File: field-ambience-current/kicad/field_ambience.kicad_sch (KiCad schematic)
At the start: 0 parts

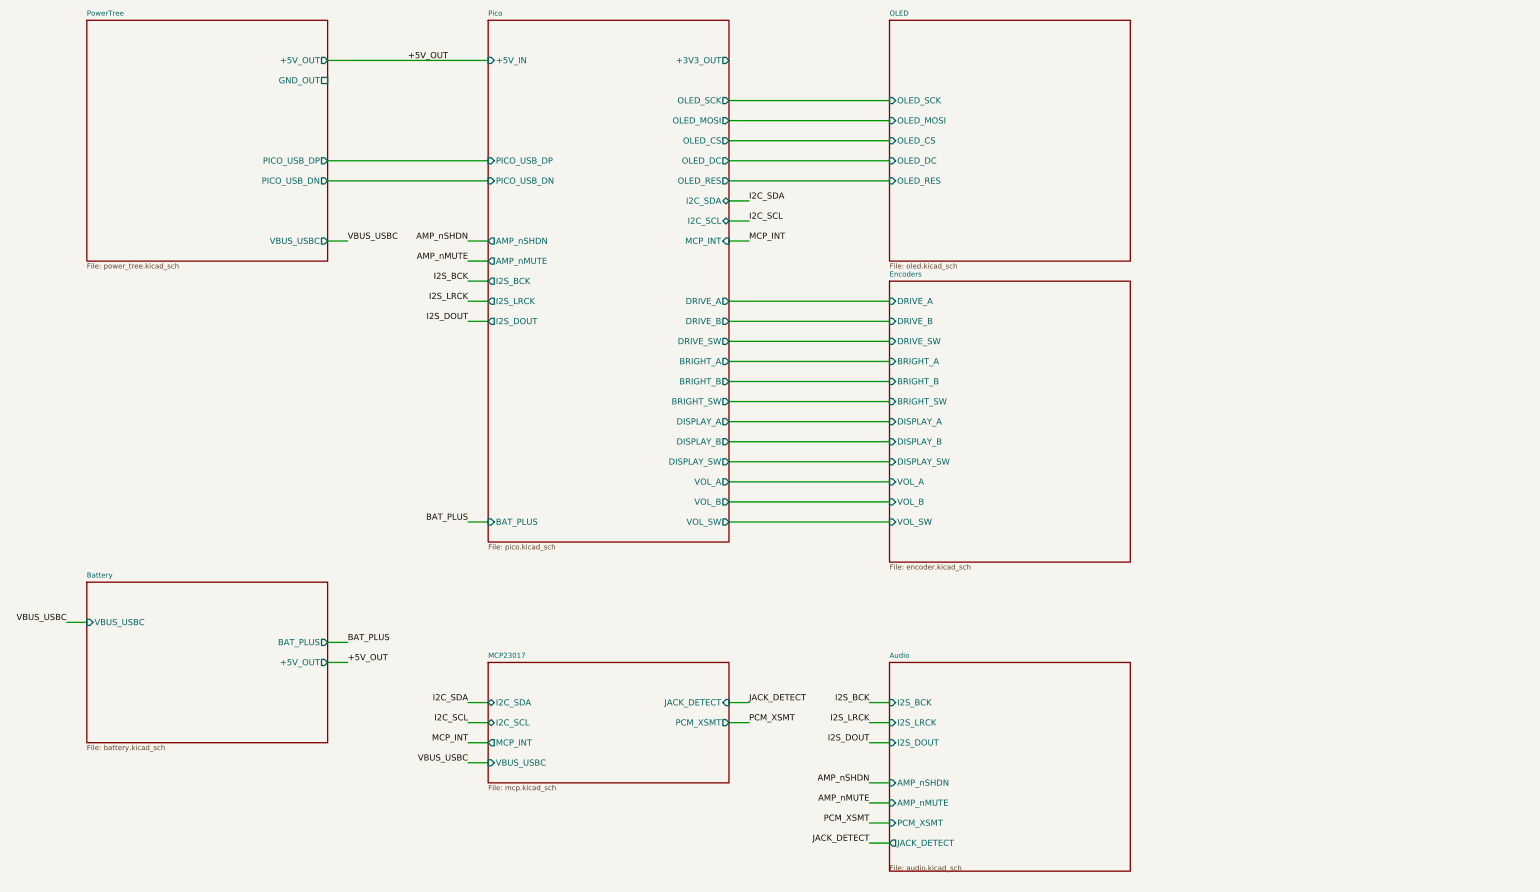
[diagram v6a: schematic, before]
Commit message: pcb(r18.5): Schematic-Migration Phase 3 — STM32H743 + LCD im Generator, Repo-Audit-Fixes
KERN: generate_kicad_project.py erzeugt jetzt die H7-Architektur.

NEU stm32h743.kicad_sch (ersetzt pico.kicad_sch -> kicad/legacy_pico2/):
- 100-Pin-Symbol 1:1 aus offizieller KiCad-Lib (MCU_ST_STM32H7),
  doppelt verifiziert gegen SPEC v0.7 §5 / DS12110 Rev 5 Table 8 —
  alle 52 belegten Zuordnungen identisch (zwei unabhängige Quellen)
- alle SPEC-§5-Netze verdrahtet, 48 Reserve-GPIOs no_connect
- Support: HSE Y1 ABLS-8.000MHZ-B4-T (C596838) + 2x22pF, VCAP 2x2.2uF
  (DS12110 Tab.24), 5x(4.7uF+100nF) VDD-Bank, VDDA-Ferrit C84094 +
  1uF+100nF, BOOT0-PD 10k, NRST-PU 10k+100nF, SWD-J4 (PA13/PA14/GND),
  BAT-Teiler 100k/100k+10nF an PA3, Status-LED PD8, USB-FS PA11/PA12
  (USBLC6-ESD bleibt davor), MIDI_TX-Netz (PD5)

NEU lcd.kicad_sch (ersetzt oled.kicad_sch -> legacy): 8-Pin-ST7789
per SPEC §6 + C6b/C6c + Backlight: PCA9685-Kanal-12 -> LCD_BLK_PWM ->
2N7002 Low-Side + 100k-PD. Netze OLED_* -> LCD_*.

power_tree: U5 AP7361A-33 LDO (+5V->+3V3) + Cin 1uF/Cout 2.2uF +
EN->IN. Pico-SMPS entfällt. PICO_USB_* -> USB_DM/USB_DP.

mcp: GPB5 = VOL_SW (SPEC §5.4 — lag bis r17 entgegen der SPEC am
Pico-GPIO), PCA-Kanal 12 = LCD_BLK_PWM. Root-Brücken umgebaut,
kicad_pro-Sheetliste: Battery ergänzt (fehlte).

AUDIT-FINDINGS (verifiziert, nicht aus dem Alt-Audit übernommen):
- F-6 NEU 🔴: SPEC-§4-U5-LCSC C156144 ist ein 910R-WIDERSTAND
  (LCSC-Web verifiziert) — hätte bei JLC einen R als LDO bestückt.
  SPEC korrigiert (Kandidat C150719), Symbol trägt TBD-VERIFY.
- B-LDO 🔴: AP7361A-SOT-89-5-Pinout-Annahme (1=ADJ/NC,2=OUT,3=IN,
  4=GND,5=EN aus AP7361-DS33626-Lesart; A-Datasheet war HTTP 403) —
  als PIN_VERIFY am Symbol + PCB_LAYOUT_STATUS dokumentiert.
- B-SW12 🔴: SW6-10 (HX 12x12) auf ~6mm-TL3342-Pattern — als
  FP_MISMATCH-Property an allen 5 Symbolen markiert.
- F-2-Teilfix: Encoder-MPN -> EC11J1525402, Bourns-PEC11R-PDF nach
  datasheets/legacy/ (falsches Teil); ALPS-Drawing offen.
- F-1: T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
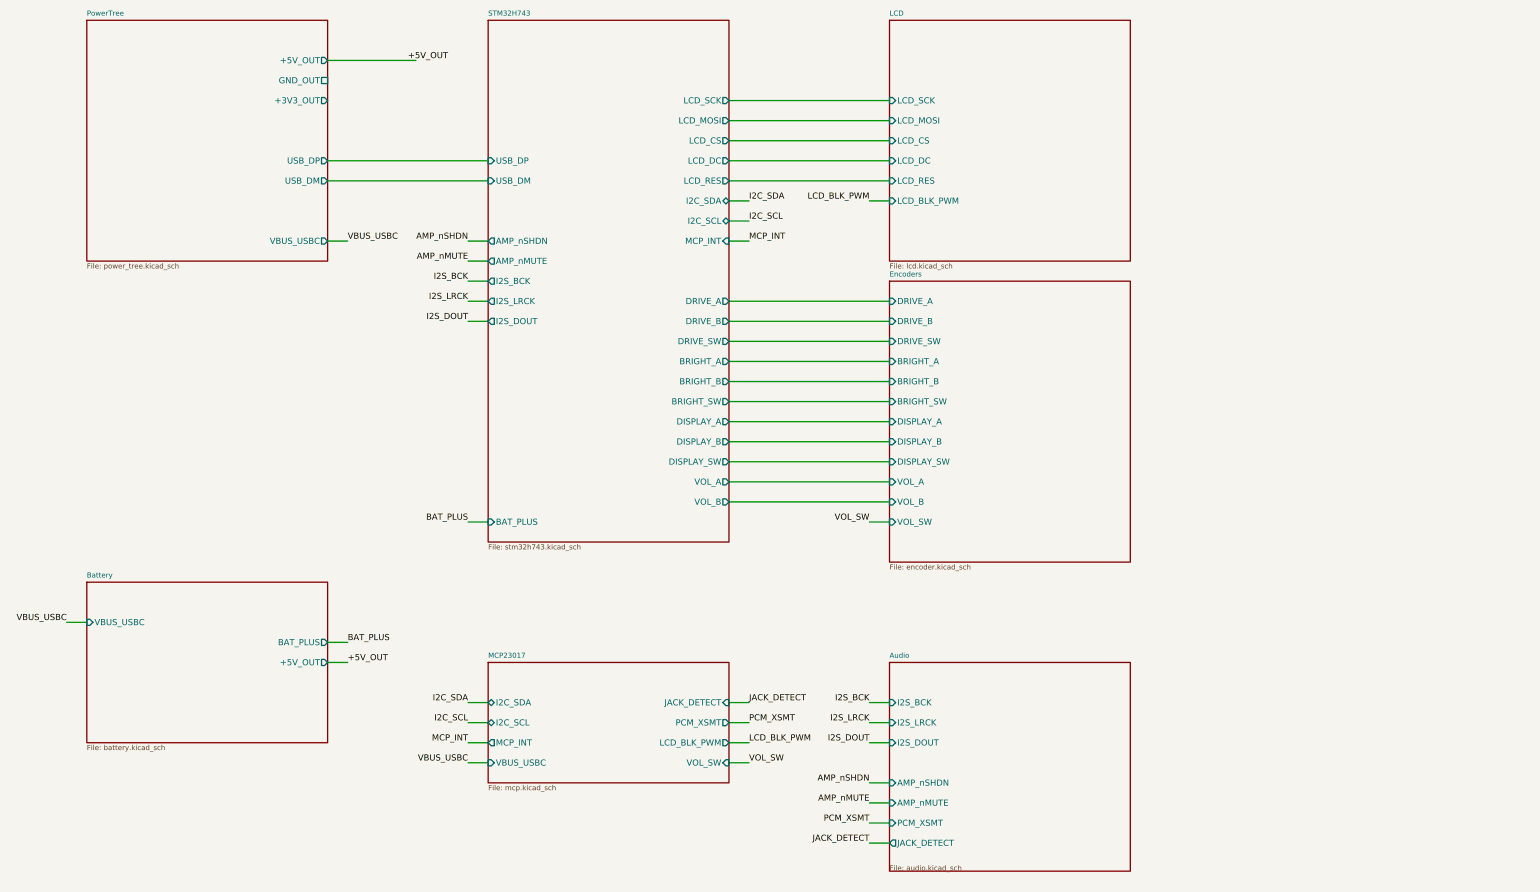
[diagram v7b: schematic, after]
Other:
- removed sheet OLED
- removed sheet Pico
- added sheet LCD (lcd.kicad_sch)
- added sheet STM32H743 (stm32h743.kicad_sch)
- sheet MCP23017 ports: added LCD_BLK_PWM, VOL_SW; removed none
- sheet PowerTree ports: added +3V3_OUT, USB_DM, USB_DP; removed PICO_USB_DN, PICO_USB_DP
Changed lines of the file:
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@@
       (effects (font (size 1.524 1.524)) (justify right))
 )
-    (pin "PICO_USB_DP" output (at 90 75 0)
-      (effects (font (size 1.524 1.524)) (justify right))
-)
-    (pin "PICO_USB_DN" output (at 90 80 0)
+    (pin "+3V3_OUT" output (at 90 60 0)
+      (effects (font (size 1.524 1.524)) (justify right))
+)
+    (pin "USB_DP" output (at 90 75 0)
+      (effects (font (size 1.524 1.524)) (justify right))
+)
+    (pin "USB_DM" output (at 90 80 0)
       (effects (font (size 1.524 1.524)) (justify right))
 )
@@
     (stroke (width 0.1524) (type solid))
     (fill (color 0 0 0 0.0000))
-    (property "Sheetname" "Pico" (at 130 39 0)
-      (effects (font (size 1.27 1.27)) (justify left bottom)))
-    (property "Sheetfile" "pico.kicad_sch" (at 130 170.5 0)
-      (effects (font (size 1.27 1.27)) (justify left top)))
-    (pin "+5V_IN" input (at 130 50 180)
-      (effects (font (size 1.524 1.524)) (justify left))
-)
-    (pin "PICO_USB_DP" input (at 130 75 180)
-      (effects (font (size 1.524 1.524)) (justify left))
-)
-    (pin "PICO_USB_DN" input (at 130 80 180)
-      (effects (font (size 1.524 1.524)) (justify left))
-)
-    (pin "+3V3_OUT" output (at 190 50 0)
-      (effects (font (size 1.524 1.524)) (justify right))
-)
-    (pin "OLED_SCK" output (at 190 60 0)
-      (effects (font (size 1.524 1.524)) (justify right))
-)
-    (pin "OLED_MOSI" output (at 190 65 0)
-      (effects (font (size 1.524 1.524)) (justify right))
-)
-    (pin "OLED_CS" output (at 190 70 0)
-      (effects (font (size 1.524 1.524)) (justify right))
-)
-    (pin "OLED_DC" output (at 190 75 0)
-      (effects (font (size 1.524 1.524)) (justify right))
-)
-    (pin "OLED_RES" output (at 190 80 0)
+    (property "Sheetname" "STM32H743" (at 130 39 0)
+      (effects (font (size 1.27 1.27)) (justify left bottom)))
+    (property "Sheetfile" "stm32h743.kicad_sch" (at 130 170.5 0)
+      (effects (font (size 1.27 1.27)) (justify left top)))
+    (pin "USB_DP" input (at 130 75 180)
+      (effects (font (size 1.524 1.524)) (justify left))
+)
+    (pin "USB_DM" input (at 130 80 180)
+      (effects (font (size 1.524 1.524)) (justify left))
+)
+    (pin "LCD_SCK" output (at 190 60 0)
+      (effects (font (size 1.524 1.524)) (justify right))
+)
+    (pin "LCD_MOSI" output (at 190 65 0)
+      (effects (font (size 1.524 1.524)) (justify right))
+)
+    (pin "LCD_CS" output (at 190 70 0)
+      (effects (font (size 1.524 1.524)) (justify right))
+)
+    (pin "LCD_DC" output (at 190 75 0)
+      (effects (font (size 1.524 1.524)) (justify right))
+)
+    (pin "LCD_RES" output (at 190 80 0)
       (effects (font (size 1.524 1.524)) (justify right))
 )
@@
       (effects (font (size 1.524 1.524)) (justify right))
 )
-    (pin "VOL_SW" output (at 190 165 0)
-      (effects (font (size 1.524 1.524)) (justify right))
-)
     (pin "AMP_nSHDN" output (at 130 95 180)
       (effects (font (size 1.524 1.524)) (justify left))
@@
     (stroke (width 0.1524) (type solid))
     (fill (color 0 0 0 0.0000))
-    (property "Sheetname" "OLED" (at 230 39 0)
-      (effects (font (size 1.27 1.27)) (justify left bottom)))
-    (property "Sheetfile" "oled.kicad_sch" (at 230 100.5 0)
-      (effects (font (size 1.27 1.27)) (justify left top)))
-    (pin "OLED_SCK" input (at 230 60 180)
-      (effects (font (size 1.524 1.524)) (justify left))
-)
-    (pin "OLED_MOSI" input (at 230 65 180)
-      (effects (font (size 1.524 1.524)) (justify left))
-)
-    (pin "OLED_CS" input (at 230 70 180)
-      (effects (font (size 1.524 1.524)) (justify left))
-)
-    (pin "OLED_DC" input (at 230 75 180)
-      (effects (font (size 1.524 1.524)) (justify left))
-)
-    (pin "OLED_RES" input (at 230 80 180)
-      (effects (font (size 1.524 1.524)) (justify left))
-))
+    (property "Sheetname" "LCD" (at 230 39 0)
+      (effects (font (size 1.27 1.27)) (justify left bottom)))
+    (property "Sheetfile" "lcd.kicad_sch" (at 230 100.5 0)
+      (effects (font (size 1.27 1.27)) (justify left top)))
+    (pin "LCD_SCK" input (at 230 60 180)
+      (effects (font (size 1.524 1.524)) (justify left))
+)
+    (pin "LCD_MOSI" input (at 230 65 180)
+      (effects (font (size 1.524 1.524)) (justify left))
+)
+    (pin "LCD_CS" input (at 230 70 180)
+      (effects (font (size 1.524 1.524)) (justify left))
+)
+    (pin "LCD_DC" input (at 230 75 180)
+      (effects (font (size 1.524 1.524)) (justify left))
+)
+    (pin "LCD_RES" input (at 230 80 180)
+      (effects (font (size 1.524 1.524)) (justify left))
+)
+    (pin "LCD_BLK_PWM" input (at 230 85 180)
+      (effects (font (size 1.524 1.524)) (justify left))
+))
+  (wire (pts (xy 225 85) (xy 230 85)) (stroke (width 0) (type default)))
+  (label "LCD_BLK_PWM" (at 225 85 0) (effects (font (size 1.524 1.524)) (justify right bottom)))
   (sheet (at 130 200) (size 60 30) (fields_autoplaced)
     (stroke (width 0.1524) (type solid))
@@
     (pin "VBUS_USBC" input (at 130 225 180)
       (effects (font (size 1.524 1.524)) (justify left))
+)
+    (pin "VOL_SW" input (at 190 225 0)
+      (effects (font (size 1.524 1.524)) (justify right))
+)
+    (pin "LCD_BLK_PWM" output (at 190 220 0)
+      (effects (font (size 1.524 1.524)) (justify right))
 ))
   (sheet (at 230 105) (size 60 70) (fields_autoplaced)
@@
       (effects (font (size 1.524 1.524)) (justify left))
 ))
-  (wire (pts (xy 90 50) (xy 130 50)) (stroke (width 0) (type default)))
+  (wire (pts (xy 90 50) (xy 112 50)) (stroke (width 0) (type default)))
   (wire (pts (xy 90 75) (xy 130 75)) (stroke (width 0) (type default)))
   (wire (pts (xy 90 80) (xy 130 80)) (stroke (width 0) (type default)))
@@
   (wire (pts (xy 190 155) (xy 230 155)) (stroke (width 0) (type default)))
   (wire (pts (xy 190 160) (xy 230 160)) (stroke (width 0) (type default)))
-  (wire (pts (xy 190 165) (xy 230 165)) (stroke (width 0) (type default)))
+  (wire (pts (xy 225 165) (xy 230 165)) (stroke (width 0) (type default)))
+  (label "VOL_SW" (at 225 165 0) (effects (font (size 1.524 1.524)) (justify right bottom)))
+  (wire (pts (xy 190 225) (xy 195 225)) (stroke (width 0) (type default)))
+  (label "VOL_SW" (at 195 225 0) (effects (font (size 1.524 1.524)) (justify left bottom)))
+  (wire (pts (xy 190 220) (xy 195 220)) (stroke (width 0) (type default)))
+  (label "LCD_BLK_PWM" (at 195 220 0) (effects (font (size 1.524 1.524)) (justify left bottom)))
   (sheet_instances
     (path "/" (page "1")))
